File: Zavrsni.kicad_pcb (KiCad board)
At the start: 2 copper layers, 37 parts, among them K1 JST-2pin-SMD, SW1 SW_Push, SW2 SW_Push

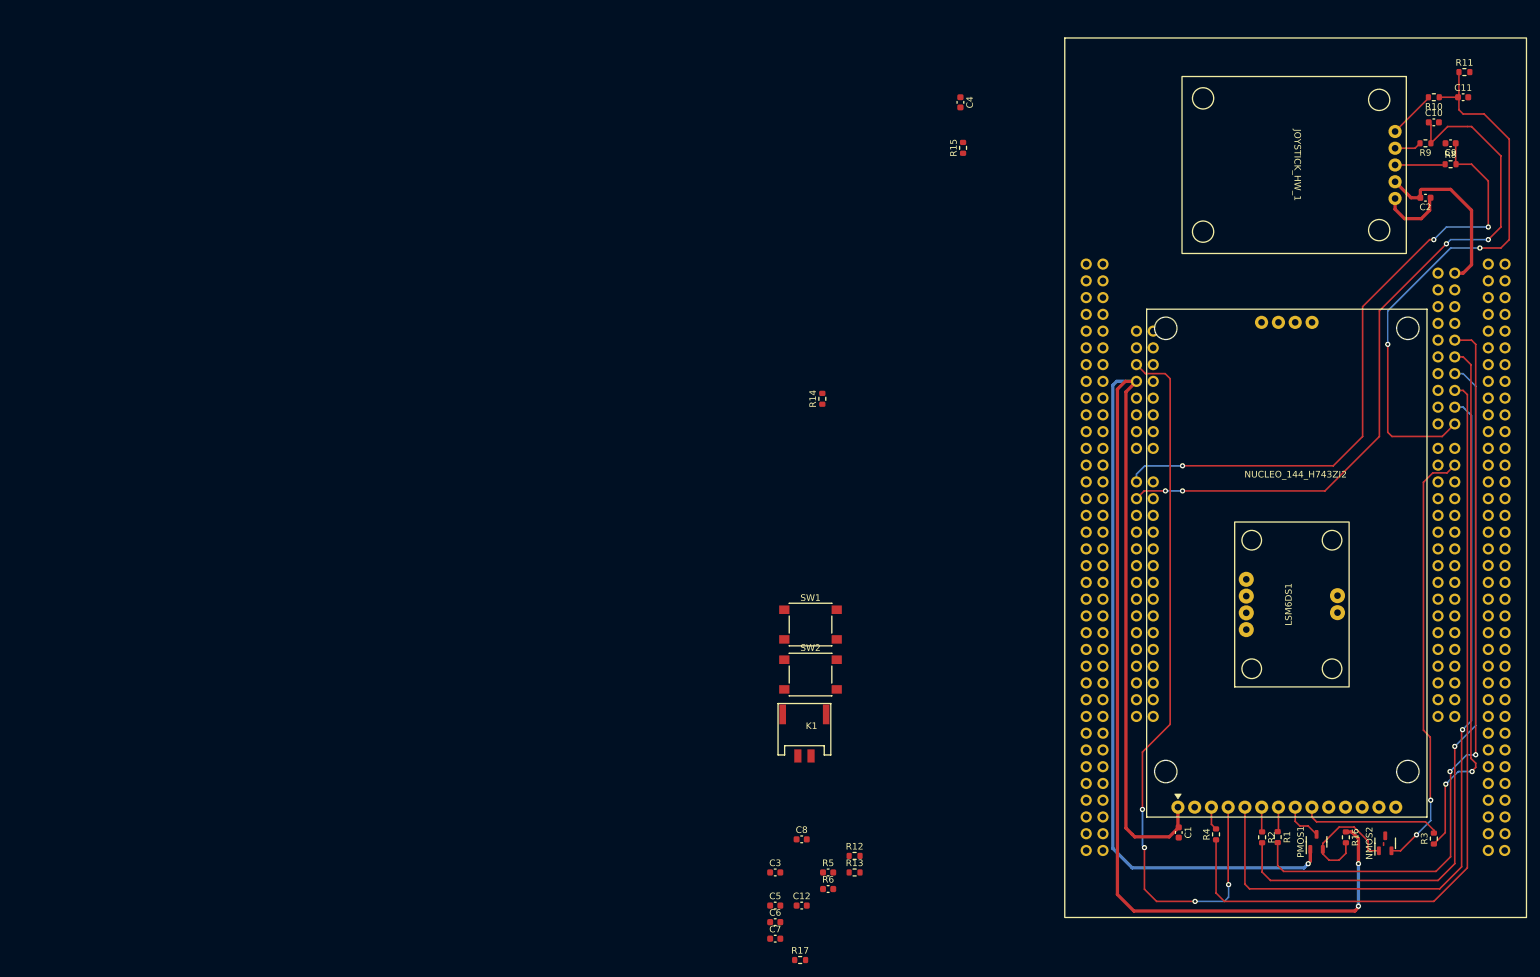
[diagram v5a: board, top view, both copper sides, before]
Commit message: [ladyM9]  LSM is placed on the bottom side of the PCB, vias are reduced, buttons are placed and connected to the PCB
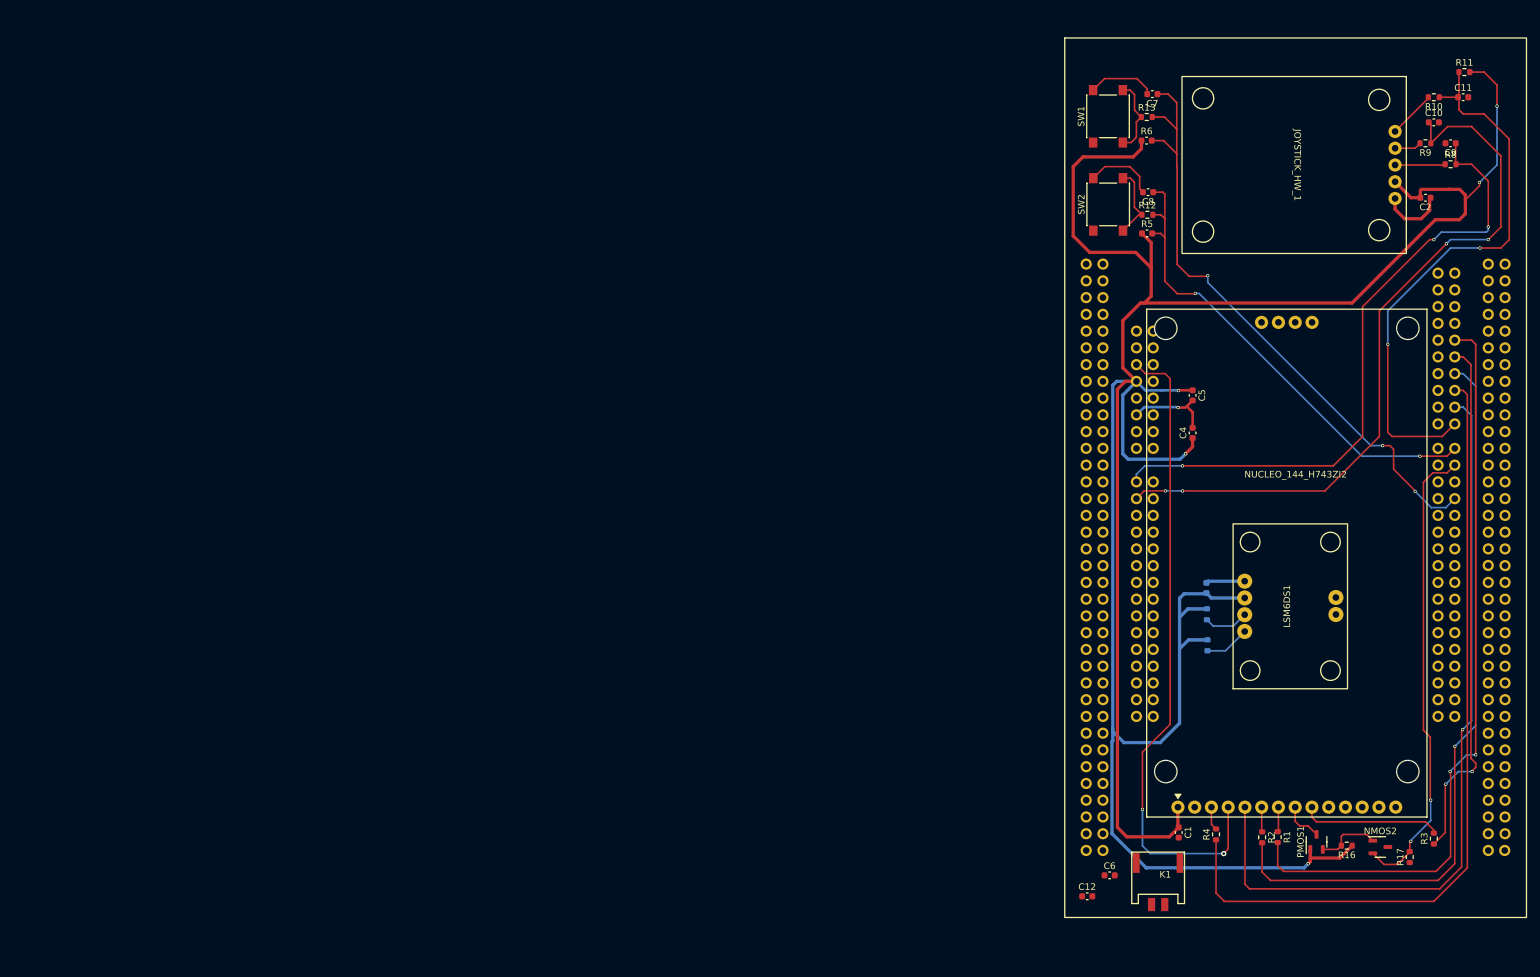
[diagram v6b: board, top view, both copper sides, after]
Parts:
- C3, R14, R15: moved to B.Cu
- moved C7 140.2 mm to (201.8, 34.5), turned to 180 degrees
- moved R6 123.3 mm to (200.9, 41.5)
- moved R13 122.8 mm to (200.9, 37.9)
- moved C8 111.3 mm to (201.2, 49.3), turned to 180 degrees
- moved R5 108.3 mm to (201.0, 55.6)
- moved R12 106.9 mm to (201.1, 52.8)
- moved C5 99.9 mm to (207.9, 80.1), turned to -90 degrees
- moved R17 93.7 mm to (240.8, 150.1), turned to 90 degrees
- moved SW1 89.3 mm to (195.1, 37.8), turned to 90 degrees
- moved SW2 84.4 mm to (195.1, 51.2), turned to 90 degrees
- moved R15 84.0 mm to (210.2, 118.0), turned to -90 degrees
- moved C3 78.3 mm to (210.0, 109.3), turned to -90 degrees
- moved R14 66.8 mm to (210.1, 113.3), turned to -90 degrees
- moved C4 61.2 mm to (207.9, 85.8), turned to 90 degrees
- moved K1 58.2 mm to (203.8, 153.3)
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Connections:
- net Net-(LSM6DS1-SCL) renamed /SCL
- net Net-(LSM6DS1-SDA) renamed /SDA
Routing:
- net /D4: track 0.00 -> 97.6 mm, vias 0 -> 3
- net +3.3V: track 346.1 -> 440.2 mm, vias 3 -> 5
- net /D7: track 0.00 -> 74.8 mm, vias 0 -> 2
- net Earth: track 10.3 -> 50.3 mm, vias 0 -> 1
- net /NRST: track 112.7 -> 98.7 mm, vias 4 -> 2
- net Net-(R13-Pad1): track 0.00 -> 11.6 mm
- net Net-(R12-Pad1): track 0.00 -> 11.3 mm
- net /D: track 19.2 -> 9.74 mm
- net /SCL: track 0.00 -> 6.86 mm
- net /SDA: track 0.00 -> 6.83 mm
- net /LED(PWM): track 65.8 -> 70.9 mm

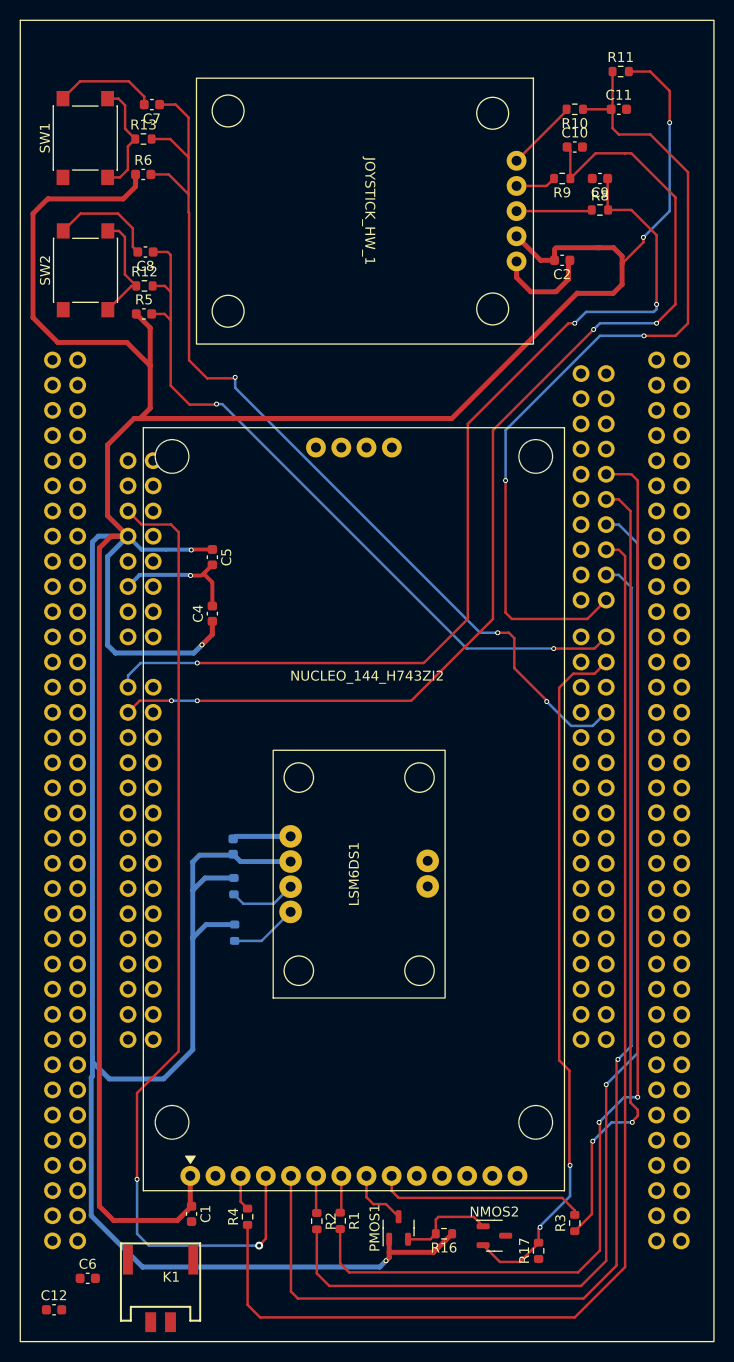
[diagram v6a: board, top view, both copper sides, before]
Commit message: All components on the PCB are connected
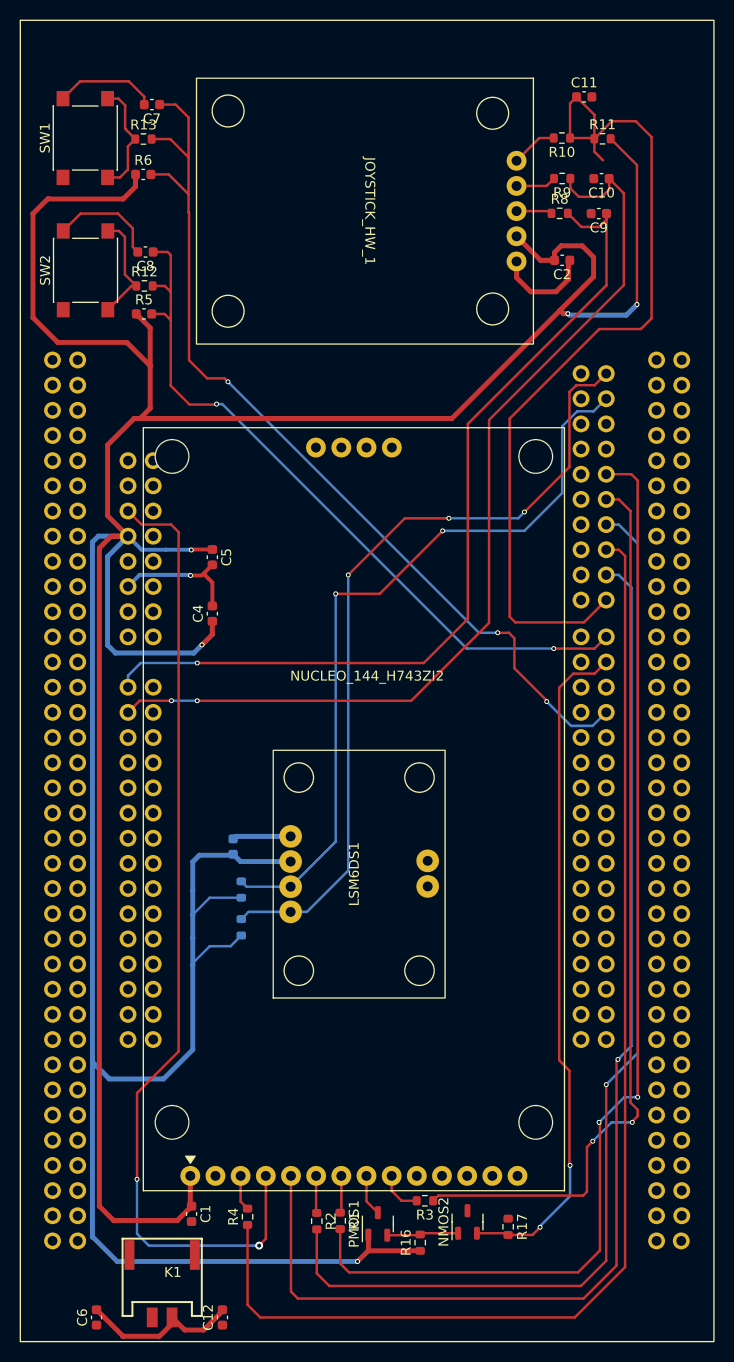
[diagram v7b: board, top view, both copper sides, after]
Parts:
- moved C12 17.0 mm to (208.9, 156.8), turned to 90 degrees
- moved R3 15.3 mm to (229.3, 145.1), turned to 180 degrees
- moved R11 7.03 mm to (247.3, 37.9)
- moved R15 4.41 mm to (210.8, 113.7)
- moved R14 4.22 mm to (210.8, 117.5), turned to 90 degrees
- moved C10 4.18 mm to (247.2, 41.9), turned to 180 degrees
- moved R8 4.08 mm to (242.9, 45.4)
- moved C6 4.04 mm to (196.2, 156.8), turned to 90 degrees
- moved R17 3.92 mm to (237.8, 147.7), turned to -90 degrees
- moved C11 3.71 mm to (245.4, 33.7)
- moved C9 3.54 mm to (246.9, 45.5)
- moved R10 3.18 mm to (243.2, 37.8)
- moved NMOS2 3.05 mm to (233.7, 147.2), turned to 90 degrees
- moved R16 2.56 mm to (228.9, 149.3), turned to 90 degrees
- moved PMOS1 2.13 mm to (224.6, 147.4)
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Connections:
- LSM6DS1 pad 3: /SDA -> /D14
- LSM6DS1 pad 4: /SCL -> /D15
- NUCLEO_144_H743ZI2 pad 48: +3.3V -> /D15
- NUCLEO_144_H743ZI2 pad 50: +3.3V -> /D14
- NUCLEO_144_H743ZI2 pad 92: (no net) -> unconnected-(NUCLEO_144_H743ZI2-PE_10-Pad92)
- R14 pad 2: /SDA -> /D15
- R15 pad 1: +3.3V -> /D14
- R15 pad 2: /SCL -> +3.3V
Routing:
- net /D15: track 0.00 -> 81.5 mm, vias 0 -> 3
- net /D14: track 0.00 -> 76.1 mm, vias 0 -> 2
- net /SDO: track 21.3 -> 4.46 mm
- net /VRy: track 111.1 -> 98.0 mm, vias 4 -> 2
- net /SDO(MISO): track 79.8 -> 91.2 mm
- net +3.3V: track 440.2 -> 451.0 mm
- net /VRx: track 98.0 -> 89.9 mm, vias 3 -> 1
- net /SCL: track 6.86 -> 0.00 mm
- net /SDA: track 6.83 -> 0.00 mm
- net /dirX: track 7.64 -> 3.62 mm
- net /SW: track 85.9 -> 89.3 mm, vias 2 -> 0
- net /T1: track 7.29 -> 4.70 mm
- net /D: track 9.74 -> 7.23 mm
- net /LED(PWM): track 70.9 -> 68.8 mm
- net /LED: track 6.21 -> 4.19 mm
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
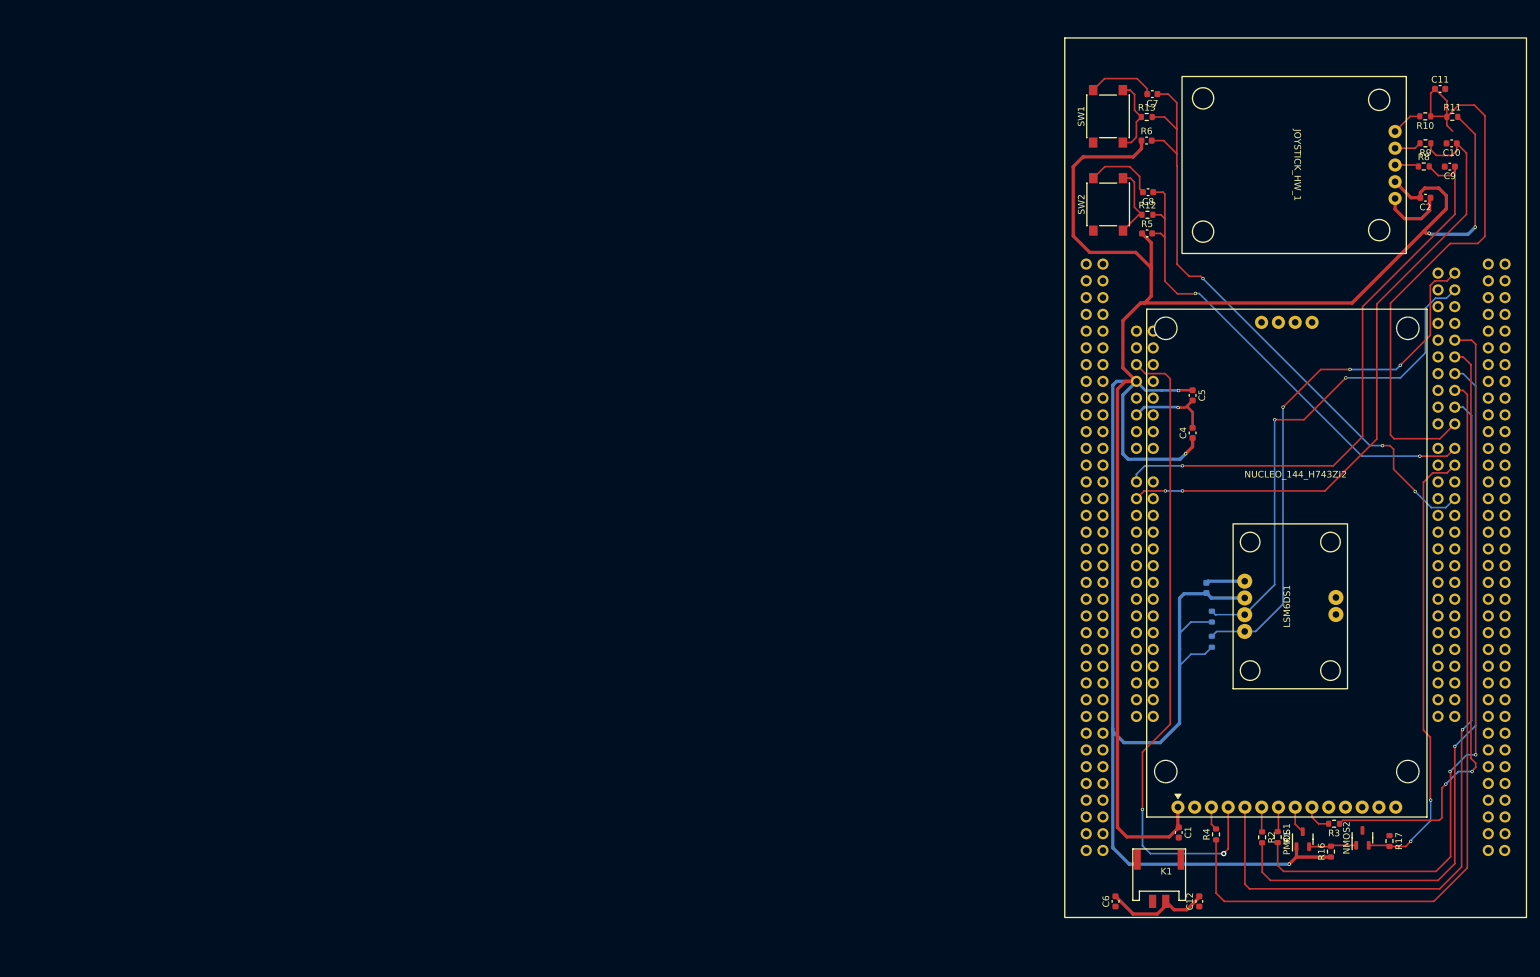
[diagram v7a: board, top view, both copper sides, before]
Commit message: Add power switch, poligon for GND, and flip lsm on bottom
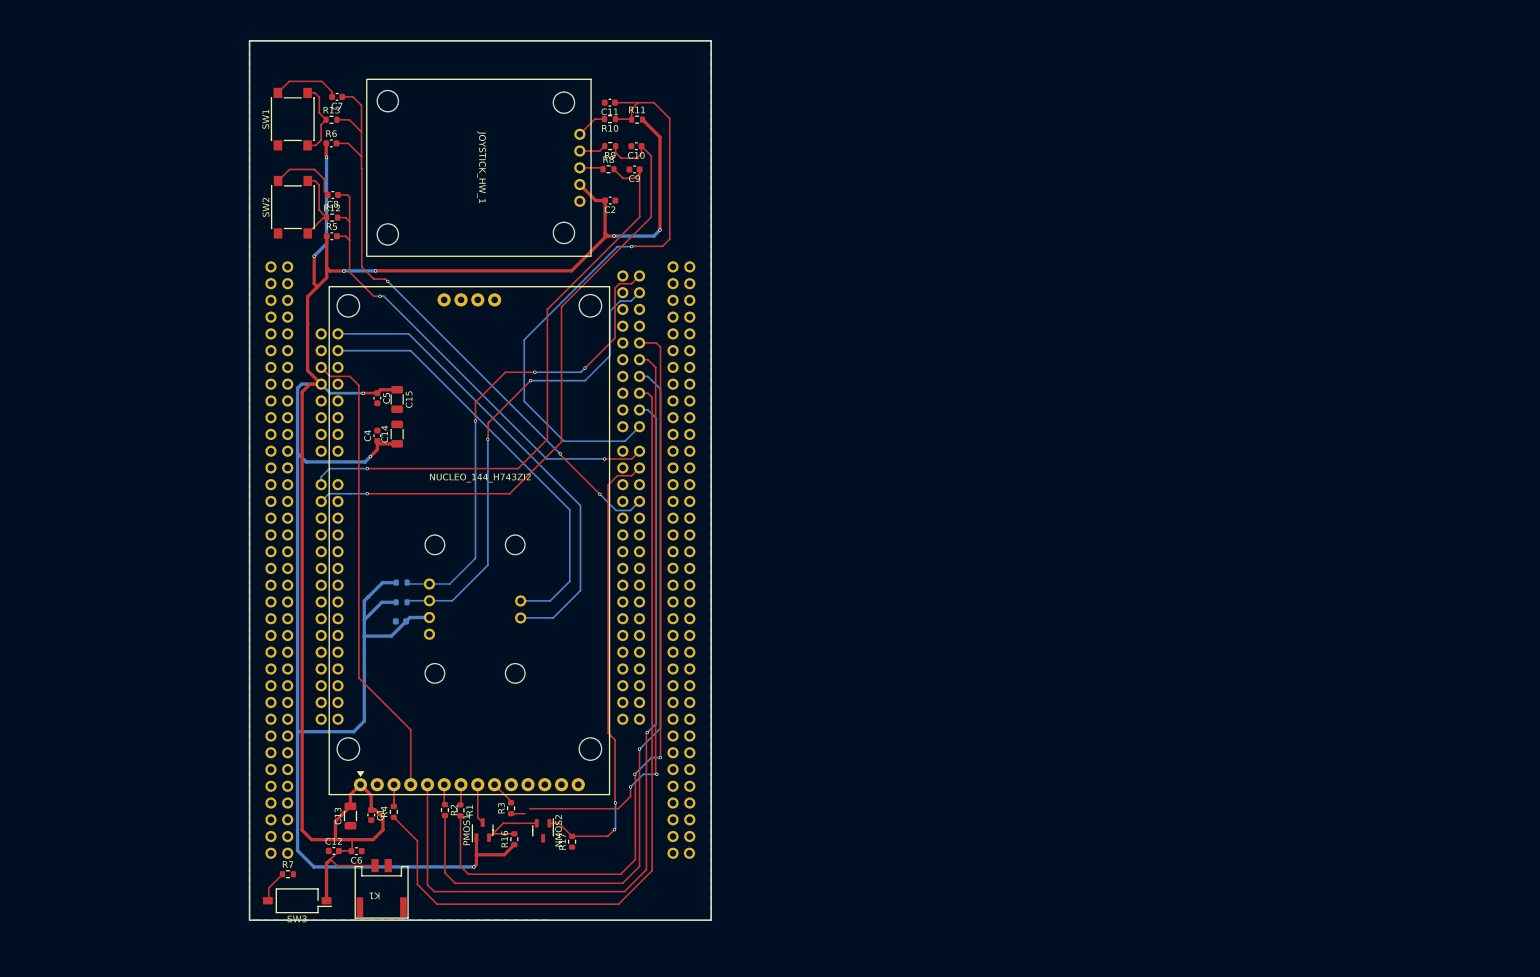
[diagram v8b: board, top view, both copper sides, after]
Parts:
- added C13: 10uF, Capacitor_SMD:C_1206_3216Metric, F.Cu at (80.2, 143.9)
- added C14: 10uF, Capacitor_SMD:C_1206_3216Metric, F.Cu at (87.3, 86.0)
- added C15: 10uF, Capacitor_SMD:C_1206_3216Metric, F.Cu at (87.3, 80.8)
- added R7: 220K, Resistor_SMD:R_0603_1608Metric, F.Cu at (70.8, 152.7)
- added SW3: Power_switch, Button_Switch_SMD:SW_DIP_SPSTx01_Slide_Omron_A6S-110x_W8.9mm_P2.54mm, F.Cu at (72.1, 156.8)
- LSM6DS1: moved to B.Cu
- moved C12 131.4 mm to (77.7, 149.2), turned to 0 degrees
- moved C11 125.9 mm to (119.5, 35.8), turned to 180 degrees
- moved R3 124.8 mm to (104.6, 142.7), turned to 90 degrees
- moved R4 124.7 mm to (86.8, 143.3)
- moved PMOS1 124.3 mm to (100.3, 146.0)
- moved NMOS2 124.2 mm to (109.4, 146.1), turned to -90 degrees
- moved DISP1 124.0 mm to (98.3, 102.2)
- moved R1 124.0 mm to (96.9, 143.1)
- moved R2 124.0 mm to (94.5, 143.0)
- moved R17 123.9 mm to (113.8, 147.8), turned to 90 degrees
- moved R16 123.8 mm to (105.1, 147.4)
- moved C10 123.6 mm to (123.6, 42.4)
- moved C2 123.6 mm to (119.6, 50.6)
- moved C4 123.6 mm to (84.3, 86.2)
- moved C5 123.6 mm to (84.3, 80.5)
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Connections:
- LSM6DS1 pad 5: unconnected-(LSM6DS1-INT1-Pad5) -> /INT1
- LSM6DS1 pad 6: unconnected-(LSM6DS1-INT2-Pad6) -> /INT2
- NMOS2 pad 1: /D -> /LED(PWM)
- NMOS2 pad 2: /LED(PWM) -> /D
- NUCLEO_144_H743ZI2 pad 10: (no net) -> unconnected-(NUCLEO_144_H743ZI2-PC12-Pad10)
- NUCLEO_144_H743ZI2 pad 12: (no net) -> unconnected-(NUCLEO_144_H743ZI2-PD2-Pad12)
- NUCLEO_144_H743ZI2 pad 14: (no net) -> unconnected-(NUCLEO_144_H743ZI2-PG2-Pad14)
- NUCLEO_144_H743ZI2 pad 16: (no net) -> unconnected-(NUCLEO_144_H743ZI2-PG3-Pad16)
- NUCLEO_144_H743ZI2 pad 18: (no net) -> unconnected-(NUCLEO_144_H743ZI2-PD7-Pad18)
- NUCLEO_144_H743ZI2 pad 2: (no net) -> /INT1
- NUCLEO_144_H743ZI2 pad 20: (no net) -> unconnected-(NUCLEO_144_H743ZI2-PD6-Pad20)
- NUCLEO_144_H743ZI2 pad 22: (no net) -> unconnected-(NUCLEO_144_H743ZI2-PD5-Pad22)
- NUCLEO_144_H743ZI2 pad 24: (no net) -> unconnected-(NUCLEO_144_H743ZI2-PD4-Pad24)
- NUCLEO_144_H743ZI2 pad 28: (no net) -> unconnected-(NUCLEO_144_H743ZI2-GND-Pad28)
- NUCLEO_144_H743ZI2 pad 4: (no net) -> /INT2
- NUCLEO_144_H743ZI2 pad 6: (no net) -> unconnected-(NUCLEO_144_H743ZI2-PC10-Pad6)
- NUCLEO_144_H743ZI2 pad 8: (no net) -> unconnected-(NUCLEO_144_H743ZI2-PC11-Pad8)
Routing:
- net /INT1: track 0.00 -> 71.2 mm
- net /INT2: track 0.00 -> 64.7 mm
- net Earth: track 50.3 -> 21.5 mm, vias 1 -> 0
- net /NRST: track 98.7 -> 70.6 mm, vias 2 -> 0
- net /D15: track 81.5 -> 72.9 mm
- net +3.3V: track 451.0 -> 445.7 mm, vias 5 -> 9
- net /D: track 7.23 -> 12.2 mm
- net Net-(R7-Pad1): track 0.00 -> 4.89 mm
- net /D14: track 76.1 -> 71.3 mm
- net /SDI(MOSI): track 112.9 -> 117.6 mm
- net /SCK(D13): track 114.7 -> 119.3 mm
- net /DC/RS: track 118.4 -> 122.4 mm
- net /SW: track 89.3 -> 91.8 mm, vias 0 -> 1
- net /SDO(MISO): track 91.2 -> 89.1 mm
- net /LED: track 4.19 -> 6.06 mm
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- added copper zone on B.Cu, net Earth
- added copper zone on F.Cu, net Earth
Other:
- board outline added: 70 x 133.3 mm
